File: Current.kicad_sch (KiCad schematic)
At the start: 120 parts, among them IC1 LM809, IC2 74HC245, IC3 74HC245, J1 Stereo Output, J3 USB_B_Mini, J4 Conn_01x20, J5 Conn_01x20, J6 Stereo Microphone, J7 External Microphone, Q1 BSS138, Q2 BSS138, Q3 BSS138, SW1 RotaryEncoder, SW2 RotaryEncoder, SW3 RotaryEncoder, SW4 SW_Push, SW5 SW_Push, SW6 SW_Push, U1 STM32F746NGHx, U2 WM8731CLSEFL, U4 LD1117S12TR_SOT223, X1 16MHz, X3 12.288MHz

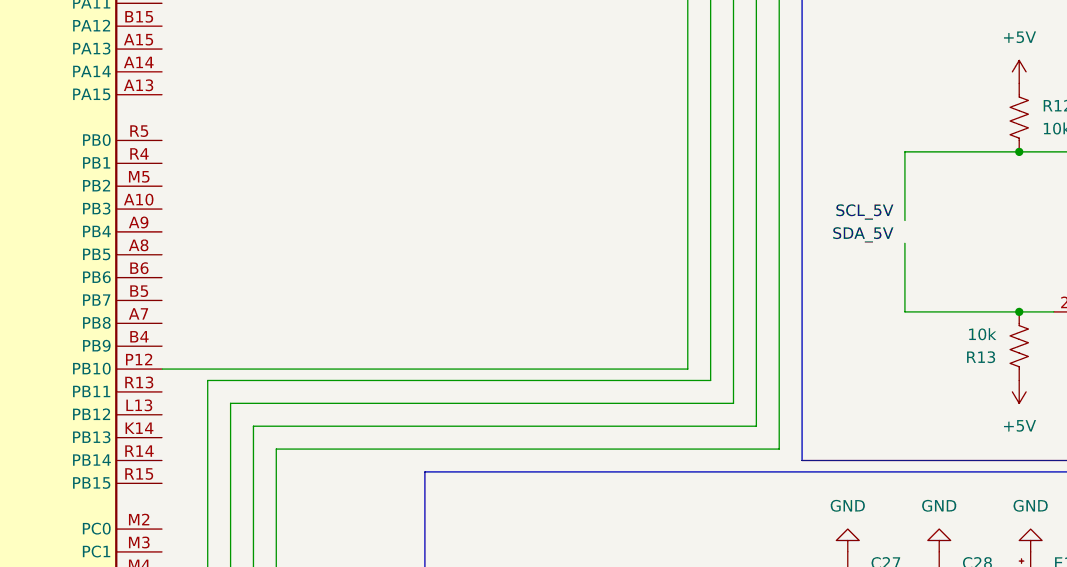
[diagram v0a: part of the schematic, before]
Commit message: Added Solder Jumpers to IC1 (PB6/PB7)
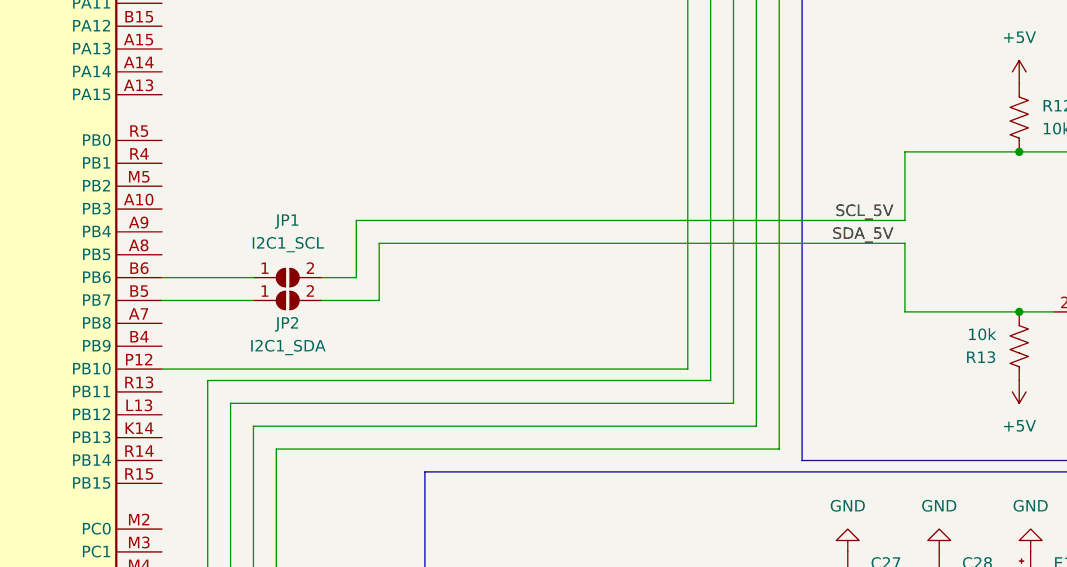
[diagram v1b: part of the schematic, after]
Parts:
- added JP1: I2C1_SCL, symbol Jumper:SolderJumper_2_Open
- added JP2: I2C1_SDA, symbol Jumper:SolderJumper_2_Open
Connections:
- net SCL_5V: now also Q2.3 (D), R12.2, JP1.2 (B)
- net SDA_5V: now also Q1.2 (S), R13.2, JP2.2 (B)
- net at U1.B5 (PB7): now also JP2.1 (A)
- net at U1.B6 (PB6): now also JP1.1 (A)

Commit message: Add files via upload
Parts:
- removed C11, C12: 20pF, symbol Device:C_Small
- removed C21, C22: 22pF, symbol Device:C_Small
- removed C29, C30, C31, C32, C33: 0.1uF, symbol Device:C
- removed C36, C37: 1nF, symbol Device:C_Small
- removed D1, D3: BZX84Cxx, Package_TO_SOT_SMD:SOT-23, symbol Diode:BZX84Cxx
- removed D6, D7: LED, symbol Device:LED
- removed E15, E8: 10uF, symbol Device:C_Polarized_Small
- removed J1: Stereo Output, symbol Connector_Audio:AudioJack3
- removed J3: USB_B_Mini, symbol Connector:USB_B_Mini
- removed J4: Conn_01x20, symbol Connector_Generic:Conn_01x20
- removed J6: Stereo Microphone, symbol Connector_Audio:AudioJack3
- removed J7: External Microphone, symbol Connector_Audio:AudioJack3
- removed L2: 10uH, symbol Device:L_Small
- removed R2, R3, R4, R5: R_Small, symbol Device:R_US
- removed R2, R5: 1k, symbol Device:R_US
- removed R3, R4: 27, symbol Device:R_US
- removed R48: 5.6k, symbol Device:R_US
- removed SW1, SW2, SW3: RotaryEncoder, symbol Device:RotaryEncoder
- removed SW4, SW5: SW_Push, symbol Switch:SW_Push
- removed SW6: SW_Push, Button_Switch_SMD:SW_SPST_PTS645, symbol Switch:SW_Push
- removed U1: STM32F746NGHx, Package_BGA:TFBGA-216_13x13mm_Layout15x15_P0.8mm, symbol MCU_ST_STM32F7:STM32F746NGHx
- removed U2: WM8731CLSEFL, Package_DFN_QFN:QFN-28-1EP_5x5mm_P0.5mm_EP3.35x3.35mm, symbol Audio:WM8731CLSEFL
- removed U4: LD1117S12TR_SOT223, Package_TO_SOT_SMD:SOT-223-3_TabPin2, symbol Regulator_Linear:LD1117S12TR_SOT223
- removed X3: 12.288MHz, symbol Device:Crystal
- added C11, C12, C22, C23: 0.1uF, ECE477Library:0.1uF, symbol Device:C
- added C21: 22uF, ECE477Library:22uF, symbol Device:C
- added C24: 20pF, ECE477Library:20pF, symbol Device:C_Small
- added C29, C30, C31: 100nF, ECE477Library:0.1uF, symbol Device:C_Small
- added C32, C33: 1nF, ECE477Library:1000pF, symbol Device:C_Small
- added D1, D3: LED, LED_SMD:LED_0201_0603Metric, symbol Device:LED
- added D6, D7: BZX84Cxx, Package_TO_SOT_SMD:SOT-23, symbol Diode:BZX84Cxx
- added E6, E7: 330uF, Capacitor_SMD:C_0201_0603Metric, symbol Device:C_Polarized_Small
- added J1: USB_OTG, ECE477Library:usb_mini, symbol Connector:USB_OTG
- added J2: Stereo Output, symbol Connector_Audio:AudioJack3
- added J3: Stereo Microphone, symbol Connector_Audio:AudioJack3
- added J4: External Microphone, symbol Connector_Audio:AudioJack3
- added J6: Conn_01x20, symbol Connector_Generic:Conn_01x20
- added L1: 10uH, symbol Device:L_Small
- added R2: 100K, Resistor_SMD:R_0201_0603Metric, symbol Device:R_US
- added R3, R4, R5: 150, Resistor_SMD:R_0201_0603Metric, symbol Device:R_US
- added R33, R34, R36, R37: 5.6k, Resistor_SMD:R_0201_0603Metric, symbol Device:R_US
- added R35: 47k, Resistor_SMD:R_0201_0603Metric, symbol Device:R_US
- added SW1, SW2, SW3: SW_Push, Button_Switch_SMD:SW_SPST_PTS645, symbol Switch:SW_Push
- added SW4, SW5, SW6: RotaryEncoder, ECE477Library:rotary_encoder, symbol Device:RotaryEncoder
- added U1: LD1117S12TR_SOT223, Package_TO_SOT_SMD:SOT-223-3_TabPin2, symbol Regulator_Linear:LD1117S12TR_SOT223
- added U2: STM32F746NGHx, Package_BGA:TFBGA-216_13x13mm_Layout15x15_P0.8mm, symbol MCU_ST_STM32F7:STM32F746NGHx
- added U3: WM8731CLSEFL, Package_DFN_QFN:QFN-28-1EP_5x5mm_P0.5mm_EP3.35x3.35mm, symbol Audio:WM8731CLSEFL
- added X2: 12.288MHz, symbol Device:Crystal
- C1, C4: value 22uF -> 0.1uF; footprint (none) -> ECE477Library:0.1uF
- C10: value .1uF -> 0.1uF; footprint Capacitor_SMD:C_0805_2012Metric_Pad1.15x1.40mm_HandSolder -> ECE477Library:0.1uF
- C13, C14, C15, C16, C17, C18, C19, C2, C28, C3, C5, C6, C7, C8: footprint (none) -> ECE477Library:0.1uF
- C20: value 0.1uF -> .1uF; footprint (none) -> ECE477Library:0.1uF
- C25: value 100nF -> 20pF; footprint (none) -> ECE477Library:20pF
- C26, C27: value 100nF -> 22pF; footprint (none) -> ECE477Library:20pF
- C34, C35: footprint (none) -> ECE477Library:1000pF
- C9: value 0.1uF -> 22uF; footprint (none) -> ECE477Library:22uF
- D2, D4, D5: footprint (none) -> LED_SMD:LED_0201_0603Metric
- E1: value 220uF -> 10uF; footprint (none) -> Capacitor_SMD:C_0201_0603Metric
- E2: footprint (none) -> Capacitor_SMD:C_0201_0603Metric
- E3: value 10uF -> 220uF; footprint (none) -> Capacitor_SMD:C_0201_0603Metric
- E4, E5: value 330uF -> 10uF; footprint (none) -> Capacitor_SMD:C_0201_0603Metric
- R1: value 1k -> 10K; footprint (none) -> Resistor_SMD:R_0201_0603Metric
- R10: value 100K -> R_Small; footprint Resistor_SMD:R_0805_2012Metric_Pad1.15x1.40mm_HandSolder -> Resistor_SMD:R_0201_0603Metric
- R11, R14, R15: value 10K -> R_Small; footprint (none) -> Resistor_SMD:R_0201_0603Metric
- R12, R13, R20: value 10k -> R_Small; footprint (none) -> Resistor_SMD:R_0201_0603Metric
- R16, R17: value 10k -> 27; footprint (none) -> Resistor_SMD:R_0201_0603Metric
- R18, R21, R27: footprint (none) -> Resistor_SMD:R_0201_0603Metric
- R19: value 2.2k -> R_Small; footprint (none) -> Resistor_SMD:R_0201_0603Metric
- R22: value 10 -> 10k; footprint (none) -> Resistor_SMD:R_0201_0603Metric
- R23: value 1 -> 10K; footprint (none) -> Resistor_SMD:R_0201_0603Metric
- R24, R25: value 10 -> R_Small; footprint (none) -> Resistor_SMD:R_0201_0603Metric
- R26: value 10k -> 10K; footprint (none) -> Resistor_SMD:R_0201_0603Metric
- R28: value 150 -> 10k; footprint (none) -> Resistor_SMD:R_0201_0603Metric
- R29: value 150 -> 330; footprint (none) -> Resistor_SMD:R_0201_0603Metric
- R30: value 150 -> 680; footprint (none) -> Resistor_SMD:R_0201_0603Metric
- R31, R32: value 150 -> 47k; footprint (none) -> Resistor_SMD:R_0201_0603Metric
- R38, R8, R9: value R_Small -> 1k; footprint (none) -> Resistor_SMD:R_0201_0603Metric
- R39: value R_Small -> 2.2k; footprint (none) -> Resistor_SMD:R_0201_0603Metric
- R40: value 330 -> 10k; footprint (none) -> Resistor_SMD:R_0201_0603Metric
- R41: value 680 -> 10k; footprint (none) -> Resistor_SMD:R_0201_0603Metric
- R42: value 47k -> 10; footprint (none) -> Resistor_SMD:R_0201_0603Metric
- R43: value 47k -> 1; footprint (none) -> Resistor_SMD:R_0201_0603Metric
- R44, R45: value 5.6k -> 10; footprint (none) -> Resistor_SMD:R_0201_0603Metric
- R46: value 47k -> 10k; footprint (none) -> Resistor_SMD:R_0201_0603Metric
- R47: value 5.6k -> 10k; footprint (none) -> Resistor_SMD:R_0201_0603Metric
- R6, R7: value R_Small -> 150; footprint (none) -> Resistor_SMD:R_0201_0603Metric
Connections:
- net +3.3V: now also C1.1, C10.1, C2.1, C26.2, E1.1, E4.2, E5.1, R1.2, R24.2, R25.1, R26.2, R31.2, R32.2, R40.2, R41.2, R46.1, R47.1, C11.1, C11.2, C12.2, C21.1, C21.2, C22.1, C22.2, C23.1, C23.2, C24.2, C29.1, C30.1, C31.1, C32.2, C33.1, D1.1 (K), D3.1 (K), D6.1 (A), D7.1 (A), J1.5 (GND), J1.6 (Shield), J2.S, J3.S, J4.S, J6.17 (Pin_17), J6.18 (Pin_18), J6.19 (Pin_19), J6.20 (Pin_20), R2.1, R33.1, R34.1, R35.2, SW1.1, SW4.C, SW5.C, SW6.C, U1.1 (GND), U1.2 (VO), U2.C1 (VBAT), U2.E10 (VDD), U2.E7 (VDD), U2.E8 (VDD), U2.E9 (VDD), U2.F10 (VSS), U2.F11 (VDD), U2.F2 (VSS), U2.F4 (VDD), U2.F5 (VDD), U2.F6 (VSS), U2.F7 (VSS), U2.F8 (VSS), U2.F9 (VSS), U2.G10 (VSS), U2.G5 (VDD), U2.G6 (VSS), U2.H10 (VSS), U2.H11 (VDD), U2.H5 (VDD), U2.H6 (VSS), U2.J10 (VSS), U2.J11 (VDD), U2.J5 (VDD), U2.J6 (VSS), U2.K10 (VSS), U2.K11 (VDD), U2.K5 (VDD), U2.K6 (VSS), U2.K7 (VSS), U2.K8 (VSS), U2.K9 (VSS), U2.L10 (VDD), U2.L6 (VSS), U2.L7 (VDD), U2.L8 (VDD), U2.L9 (VDD), U2.M1 (VSSA), U2.R1 (VDDA), U3.15 (HPGND), U3.19 (AGND), U3.25 (MODE), U3.26 (~{CSB}), U3.29 (AGND), U3.4 (DGND); no longer C20.1, C26.1, C35.1, C9.1, E3.2, J5.17 (Pin_17), J5.18 (Pin_18), J5.19 (Pin_19), J5.20 (Pin_20), R10.1, R11.2, R15.2, R20.2, R21.2, R26.1, R27.1, R42.2, R43.2, R44.1, R45.1, R46.2, R8.2, R9.1
- net +5V: now also C9.1, R21.1, R22.1, R27.1, R28.1, R38.1, C12.1, J1.1 (VBUS), U1.3 (VI); no longer R12.1, R13.1, R16.1, R17.1, R18.1
- net CTP_IRQ: now also J6.8 (Pin_8); no longer J5.8 (Pin_8)
- net DB0: now also J5.7 (Pin_7)
- net DB1: now also J5.8 (Pin_8)
- net DB2: now also J5.9 (Pin_9)
- net DB3: now also J5.10 (Pin_10)
- net DB4: now also J5.11 (Pin_11)
- net DB5: now also J5.12 (Pin_12)
- net DB6: now also J5.13 (Pin_13)
- net DB7: now also J5.14 (Pin_14)
- net IM0: now also R47.2, J6.1 (Pin_1); no longer J5.1 (Pin_1), R27.2
- net IM1: now also R46.2, J6.2 (Pin_2); no longer J5.2 (Pin_2), R26.2
- net IM2: now also R41.1, J6.3 (Pin_3); no longer J5.3 (Pin_3), R21.1
- net IM3: now also R40.1, J6.4 (Pin_4); no longer J5.4 (Pin_4), R20.1
- net LCD_CS: now also J5.1 (Pin_1)
- net LCD_CS_5V: now also R7.2, U2.F14 (PC9); no longer R32.2
- net LCD_RD: now also J5.4 (Pin_4)
- net LCD_RD_5V: now also R26.1; no longer R15.1
- net LCD_RS: now also J5.2 (Pin_2)
- net LCD_RST: now also J6.5 (Pin_5); no longer J5.5 (Pin_5)
- net LCD_RST_5V: now also R23.2, R5.2, U2.H15 (PC6); no longer R14.2, R31.2
- net LCD_RS_5V: now also R3.2, U2.P12 (PB10); no longer R29.2
- net LCD_WR: now also J5.3 (Pin_3)
- net LCD_WR_5V: now also R6.2, U2.G14 (PC8); no longer R30.2
- net LEDA: now also R42.2, R43.2, R44.2, R45.2, J6.10 (Pin_10), J6.11 (Pin_11), J6.12 (Pin_12), J6.13 (Pin_13); no longer J5.10 (Pin_10), J5.11 (Pin_11), J5.12 (Pin_12), J5.13 (Pin_13), R22.2, R23.2, R24.2, R25.2
- net LEDK: now also J6.9 (Pin_9); no longer J5.9 (Pin_9)
- net PA6(TIM3-CH1): now also R12.2, SW5.A, U2.P3 (PA6)
- net PC3: now also R4.2, U2.L4 (PC3); no longer R28.2
- net PC7(TIM3-CH2): now also R13.2, SW5.B, U2.G15 (PC7); no longer R6.2
- net PD12(TIM4-CH1): now also R14.2, SW6.A, U2.M10 (PD12)
- net PD13(TIM1-CH2): now also R15.2, SW6.B, U2.M11 (PD13)
- net PE11(TIM1-CH2): now also R11.2, SW4.B, U2.P10 (PE11), U2.R9 (PE10); no longer R7.2
- net PE3(SA1_SD_B / MISO): now also R17.2, U2.A2 (PE3)
- net PE4(SAI1_FS_A / ADCL): now also U2.A1 (PE4), U3.11 (ADCLRC), U3.9 (DACLRC)
- net PE5(SAI1_SCK_A / SCK): now also R16.2, U2.B1 (PE5)
- net PE6(SA1_SD_A / MOSI): now also R18.2, U2.B2 (PE6)
- net PE9(TIM1-CH1): now also R10.2, SW4.A, U2.N9 (PE8), U2.P9 (PE9)
- net PF0(I2C2_SDA / SDA): now also R8.2, U2.D2 (PF0), U3.27 (SDIN)
- net PF1(I2C2_SCL / SCL): now also R9.2, U2.E2 (PF1), U3.28 (SCLK); no longer R1.2
- net PF2(GPIO_Input): now also SW2.1, U2.G2 (PF2)
- net PF3(GPIO_Input): now also SW3.1, U2.H2 (PF3)
- net SCL_3V: now also R27.2, J6.6 (Pin_6); no longer J5.6 (Pin_6), R16.2
- net SCL_5V: now also R21.2; no longer R12.2
- net SDA_3V: now also R28.2, J6.7 (Pin_7); no longer J5.7 (Pin_7), R17.2
- net SDA_5V: now also R22.2; no longer R13.2
- net SDI: now also J5.5 (Pin_5)
- net SDO: now also J5.6 (Pin_6)
- net VCC: now also R20.2, R25.2, R42.1, R43.1, R44.1, R45.1, J6.14 (Pin_14), J6.15 (Pin_15), J6.16 (Pin_16); no longer J5.14 (Pin_14), J5.15 (Pin_15), J5.16 (Pin_16), R14.1, R22.1, R25.1, R38.2, R8.1, R9.2
- net VCC-3.3: now also E1.2, E5.2, R8.1, R9.1, C29.2, C30.2, C31.2, L1.1, L1.2, U3.12 (HPVDD), U3.18 (AVDD), U3.3 (DCVDD), U3.5 (DBVDD); no longer C25.2, C26.2, C27.2, R1.1
- net at E2.2: now also C33.2, R33.2, R36.2; no longer R45.2
- net at R30.1: now also U3.21 (MICBIAS); no longer D2.2 (A)
- net at JP2.1 (A): now also U2.B5 (PB7)
- net at R32.1: now also E6.2, J2.T
- net at R7.1: now also D5.2 (A)
- net at R29.1: now also U3.22 (MICIN); no longer D4.2 (A)
- net at E3.1: now also U3.23 (RLINEIN)
- net at JP1.1 (A): now also U2.B6 (PB6)
- net at R39.1: now also Q3.1 (G), R38.2
- net at E4.1: now also U3.20 (VMID)
- net at X1.1: now also C24.1, U2.H1 (PH1)
- net at X1.2: now also C25.2, U2.G1 (PH0)
- net at E2.1: now also U3.24 (LLINEIN)
- net at R6.1: now also D4.2 (A)
- net at R31.1: now also E7.2, J2.R
- new net: C27.2, U3.2 (XTO), X2.1
- new net: C34.1, E3.2, R34.2, R37.1
- new net: J3.R, R37.2
- new net: C26.1, U3.1 (XTI/MCLK), X2.2
- new net: R17.1, U3.10 (ADCDAT)
- new net: E6.1, U3.13 (LHPOUT)
- new net: E7.1, U3.14 (RHPOUT)
- new net: R16.1, U3.7 (BCLK)
- new net: R18.1, U3.8 (DACDAT)
- new net: D7.3 (K), R20.1, SW3.2
- new net: D3.2 (A), R5.1
- new net: D6.3 (K), R19.1, SW2.2
- new net: C20.1, R2.2, SW1.2, U2.J1 (NRST)
- new net: J3.T, R36.1
- new net: D2.2 (A), R4.1
- new net: C32.1, C35.2, J4.T, R30.2, R35.1
- new net: D1.2 (A), R3.1
- new net: R1.1, U2.E6 (BOOT0)
- new net: C35.1, R29.2
- no-connect marks 0 -> 3

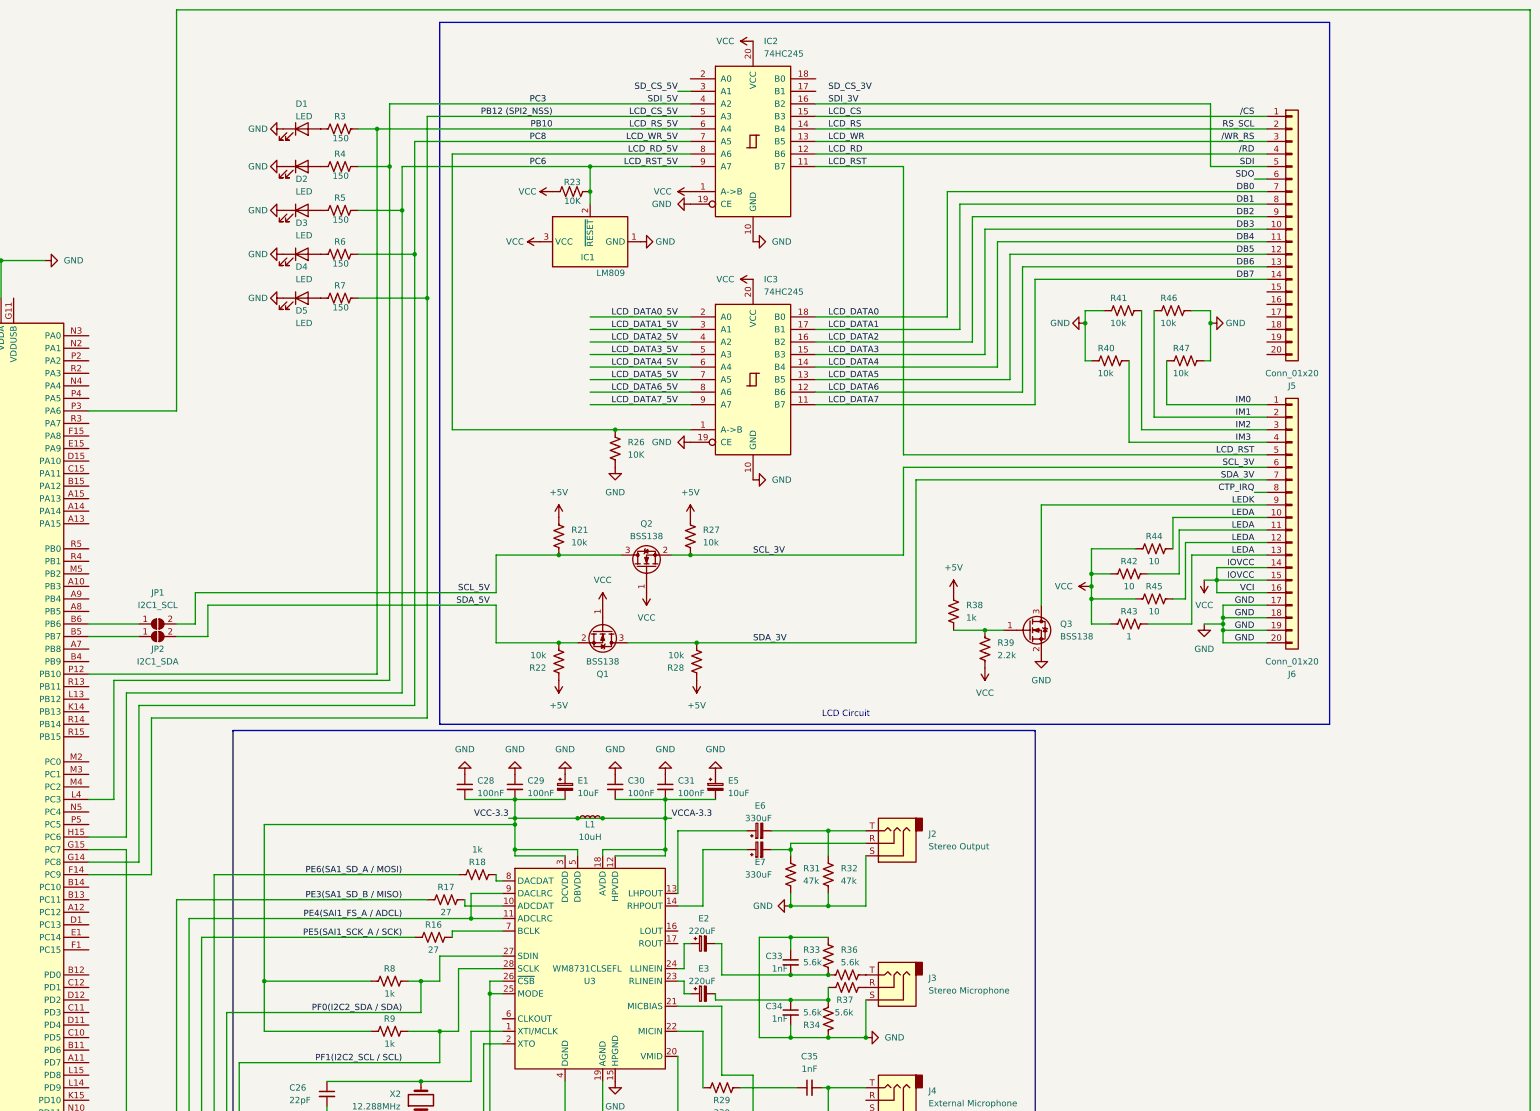
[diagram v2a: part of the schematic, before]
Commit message: Added missing footprints and redid LCD connector
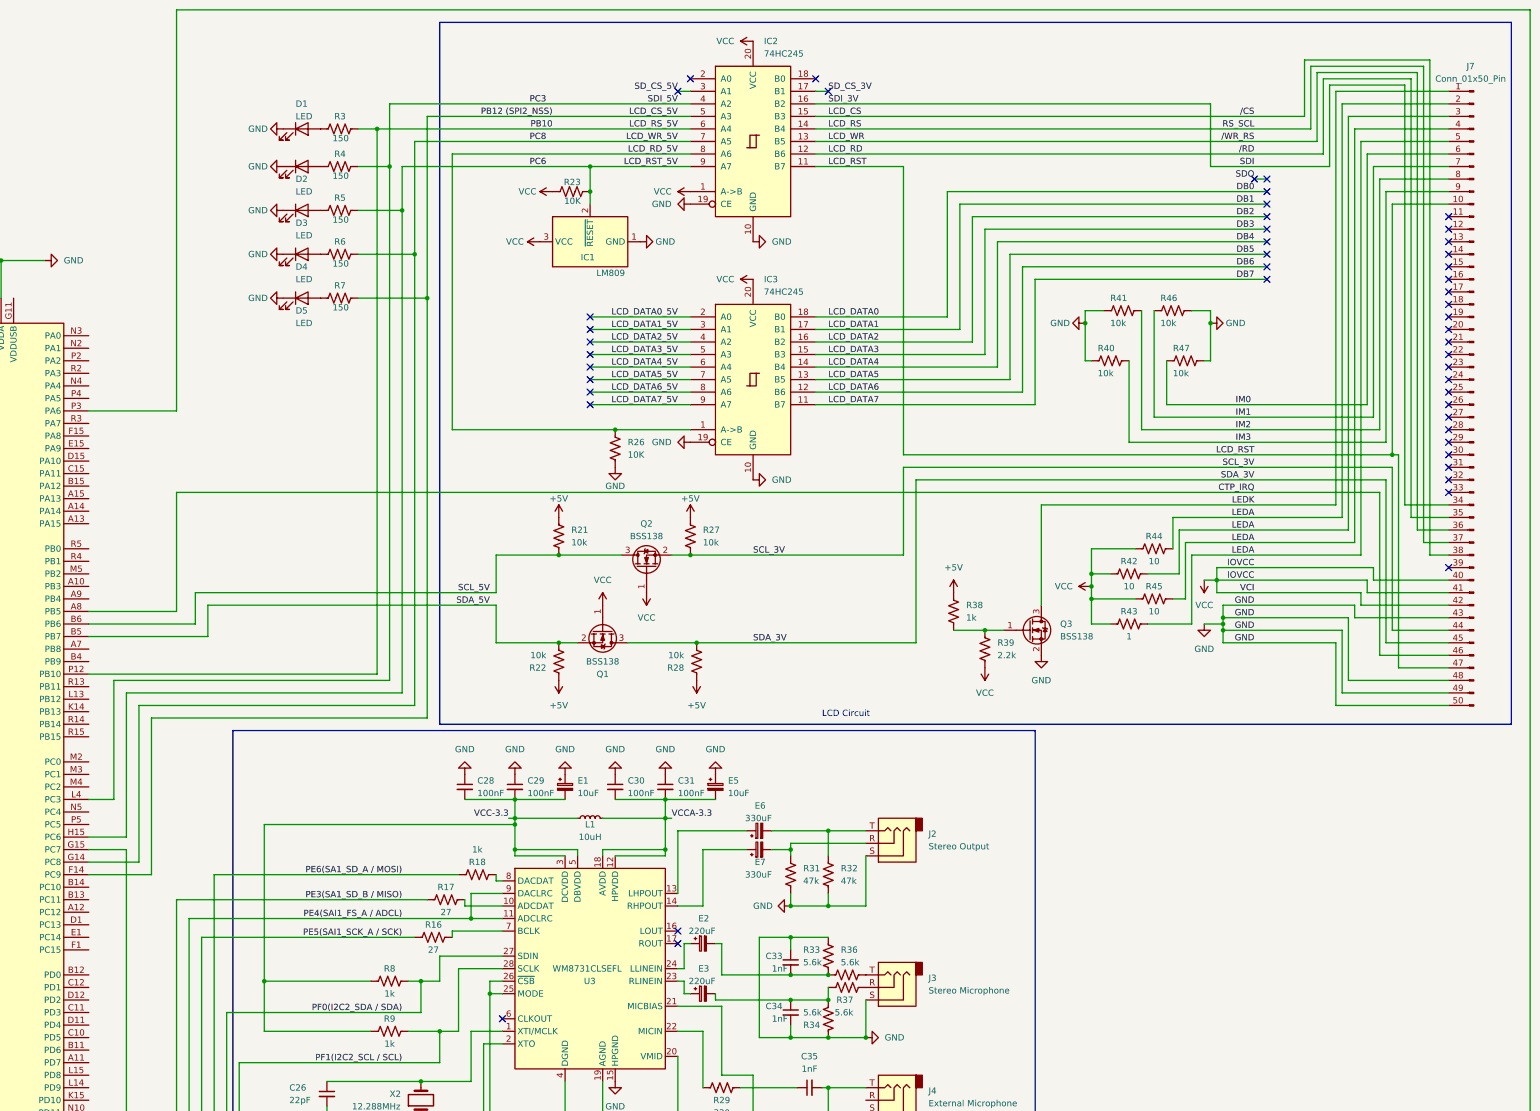
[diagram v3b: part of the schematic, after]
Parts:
- removed J5, J6: Conn_01x20, symbol Connector_Generic:Conn_01x20
- removed JP1: I2C1_SCL, symbol Jumper:SolderJumper_2_Open
- removed JP2: I2C1_SDA, symbol Jumper:SolderJumper_2_Open
- added J7: Conn_01x50_Pin, 50 Position FPC Connector Contacts:68715014522, symbol Connector:Conn_01x50_Pin
- IC2, IC3: footprint (none) -> SN74LVC245APW:SOP65P640X120-20N
- J2, J3, J4: footprint (none) -> SJ1_3515_SMT_TR:CUI_SJ1-3515-SMT
- L1: footprint (none) -> Inductor_SMD:L_0201_0603Metric_Pad0.64x0.40mm_HandSolder
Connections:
- net +3.3V: now also J7.43 (Pin_43), J7.48 (Pin_48), J7.49 (Pin_49), J7.50 (Pin_50)
- net CTP_IRQ: now also U2.A8 (PB5), J7.46 (Pin_46)
- net IM0: now also J7.6 (Pin_6)
- net IM1: now also J7.7 (Pin_7)
- net IM2: now also J7.8 (Pin_8)
- net IM3: now also J7.9 (Pin_9)
- net LCD_CS: now also J7.38 (Pin_38)
- net LCD_RD: now also J7.35 (Pin_35)
- net LCD_RS: now also J7.37 (Pin_37)
- net LCD_RST: now also J7.10 (Pin_10), J7.47 (Pin_47)
- net LCD_WR: now also J7.36 (Pin_36)
- net LEDA: now also J7.2 (Pin_2), J7.3 (Pin_3), J7.4 (Pin_4), J7.5 (Pin_5)
- net LEDK: now also J7.1 (Pin_1)
- net SCL_3V: now also J7.44 (Pin_44)
- net SCL_5V: now also U2.B6 (PB6)
- net SDA_3V: now also J7.45 (Pin_45)
- net SDA_5V: now also U2.B5 (PB7)
- net SDI: now also J7.34 (Pin_34)
- net SD_CS_3V: now also IC2.17 (B1)
- net VCC: now also J7.40 (Pin_40), J7.41 (Pin_41), J7.42 (Pin_42)
- net VCC-3.3: no longer C30.2, C31.2, E5.2, L1.2, U3.12 (HPVDD), U3.18 (AVDD)
- new net VCCA-3.3: C30.2, C31.2, E5.2, L1.2, U3.12 (HPVDD), U3.18 (AVDD)
- no-connect marks 3 -> 52

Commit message: Add files via upload
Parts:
- added D10, D11, D12, D13, D8, D9: BZX84Cxx, Package_TO_SOT_SMD:SOT-23, symbol Diode:BZX84Cxx
- added R48, R49, R50, R51, R52, R53: 220, Resistor_SMD:R_0201_0603Metric, symbol Device:R_US
- R10, R11, R12, R13, R14, R15: value R_Small -> 1k
- R19, R20: value R_Small -> 220
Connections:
- net +3.3V: now also D10.1 (A), D11.1 (A), D12.1 (A), D13.1 (A), D8.1 (A), D9.1 (A)
- net PA6(TIM3-CH1): now also R50.1; no longer SW5.A
- net PC7(TIM3-CH2): now also R51.1; no longer SW5.B
- net PD12(TIM4-CH1): now also R48.1; no longer SW6.A
- net PD13(TIM1-CH2): now also R49.1; no longer SW6.B
- net PE11(TIM1-CH2): now also R53.1; no longer SW4.B
- net PE9(TIM1-CH1): now also R52.1; no longer SW4.A
- net VCC: now also R10.1, R11.1, R12.1, R13.1, R14.1, R15.1
- new net: D8.3 (K), R48.2, SW6.A
- new net: D10.3 (K), R50.2, SW5.A
- new net: D11.3 (K), R51.2, SW5.B
- new net: D9.3 (K), R49.2, SW6.B
- new net: D12.3 (K), R52.2, SW4.A
- new net: D13.3 (K), R53.2, SW4.B
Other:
- moved on the sheet: SW4, SW5, SW6

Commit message: Add files via upload
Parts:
- E2, E3: value 220uF -> 1uF
- R24, R25: value R_Small -> 1k
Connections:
- no-connect marks 52 -> 200
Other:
- note added: "SDO"
